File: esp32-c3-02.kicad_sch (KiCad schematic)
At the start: 30 parts, among them J3 GSD090012SEU, U3 ESP32-C3-WROOM-02-H4, U4 CP2102N-Axx-xQFN20, U5 USBLC6-2SC6, U6 W25Q32JVSSIQ

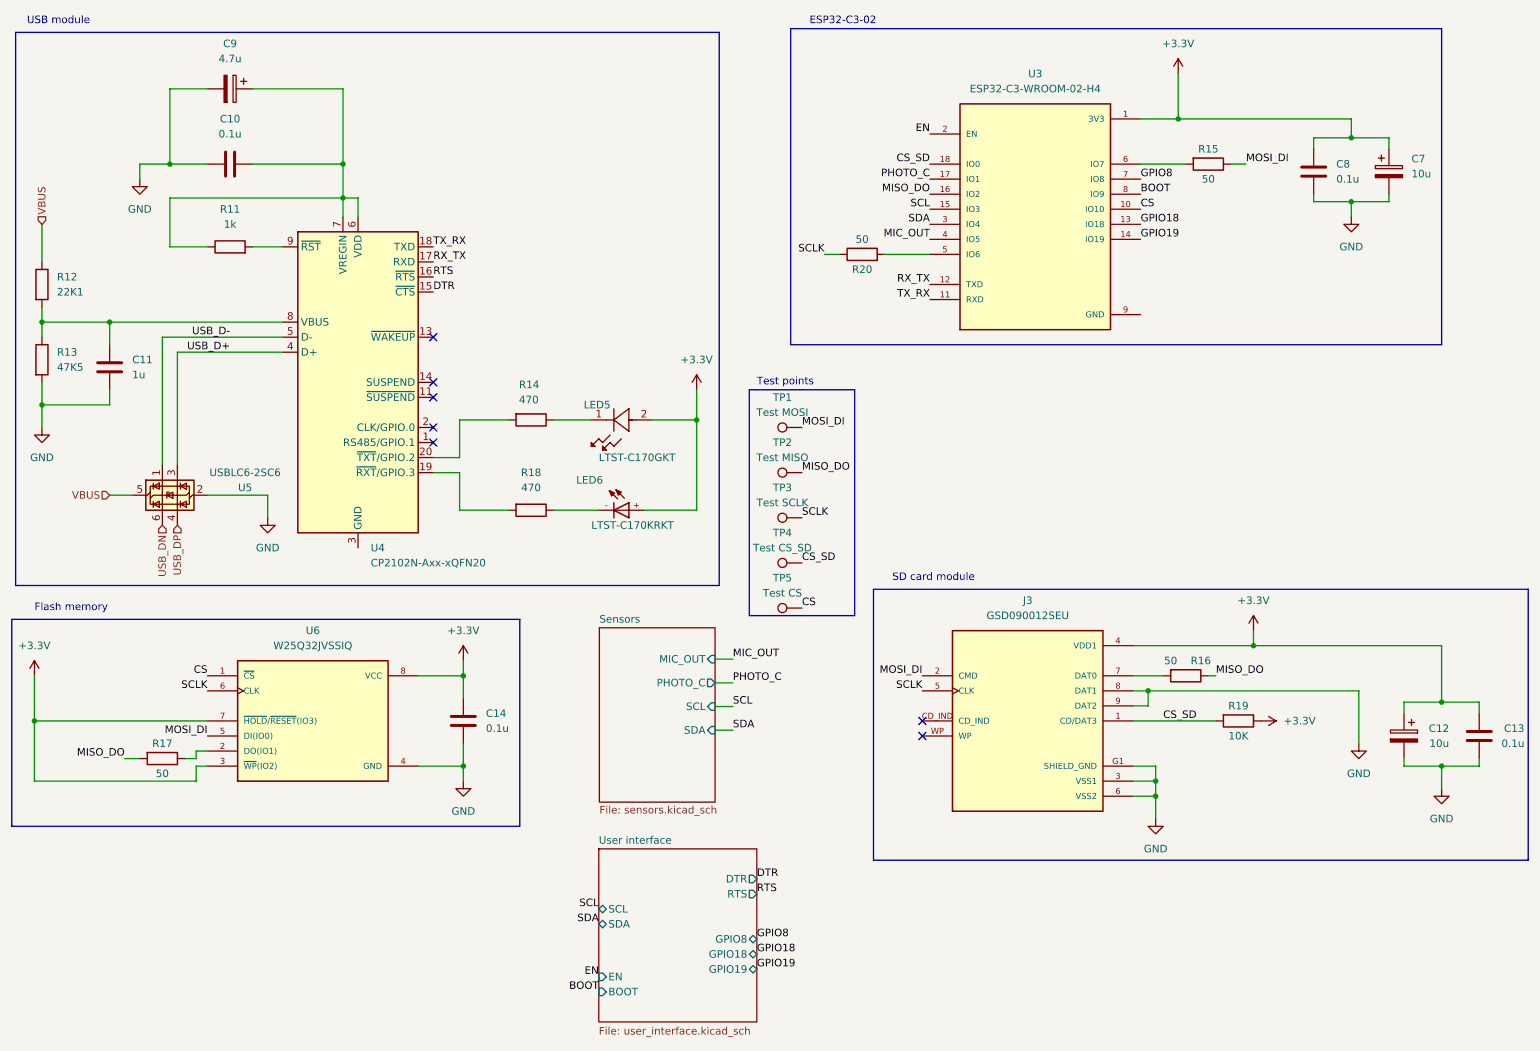
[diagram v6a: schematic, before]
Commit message: 1.3.4 Electrical Rules Check
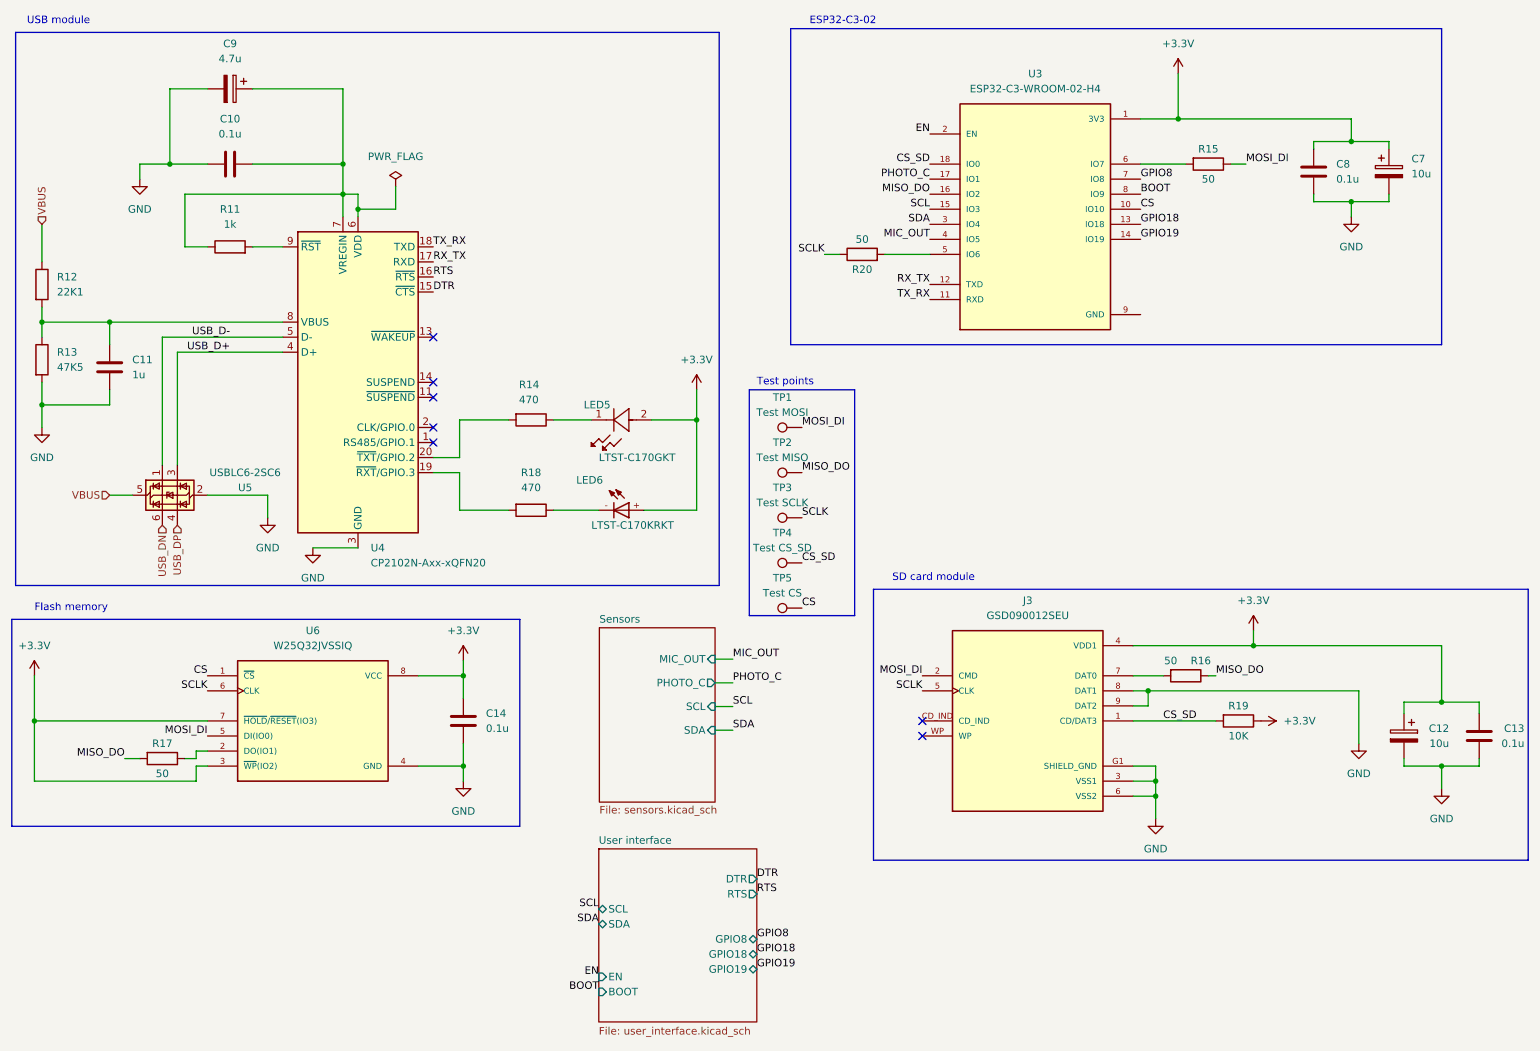
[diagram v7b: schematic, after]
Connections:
- net GND: now also U4.12 (GND), U4.21 (GND), U4.3 (GND)
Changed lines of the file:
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@@
 	)
 	(junction
-		(at 76.2 50.165)
-		(diameter 0)
-		(color 0 0 0 0)
-	)
-	(junction
 		(at 24.13 138.43)
 		(diameter 0)
@@
 	)
 	(junction
+		(at 78.74 52.07)
+		(diameter 0)
+		(color 0 0 0 0)
+	)
+	(junction
 		(at 213.36 148.59)
 		(diameter 0)
@@
 	)
 	(junction
-		(at 246.38 40.005)
+		(at 246.38 40.64)
 		(diameter 0)
 		(color 0 0 0 0)
@@
 	)
 	(junction
+		(at 76.2 49.53)
+		(diameter 0)
+		(color 0 0 0 0)
+	)
+	(junction
 		(at 135.89 87.63)
 		(diameter 0)
@@
 	(wire
 		(pts
+			(xy 76.2 49.53) (xy 76.2 53.34)
+		)
+		(stroke
+			(width 0)
+			(type default)
+		)
+	)
+	(wire
+		(pts
 			(xy 247.65 142.24) (xy 247.65 133.35)
 		)
@@
 	(wire
 		(pts
-			(xy 76.2 50.165) (xy 46.99 50.165)
+			(xy 76.2 49.53) (xy 49.53 49.53)
 		)
 		(stroke
@@
 	(wire
 		(pts
-			(xy 240.03 40.005) (xy 240.03 41.91)
+			(xy 240.03 40.64) (xy 240.03 41.91)
 		)
 		(stroke
@@
 	(wire
 		(pts
-			(xy 252.73 40.005) (xy 252.73 41.91)
+			(xy 252.73 40.64) (xy 252.73 41.91)
 		)
 		(stroke
@@
 	(wire
 		(pts
-			(xy 46.99 58.42) (xy 53.34 58.42)
+			(xy 49.53 58.42) (xy 53.34 58.42)
 		)
 		(stroke
@@
 	(wire
 		(pts
-			(xy 46.99 50.165) (xy 46.99 58.42)
+			(xy 49.53 49.53) (xy 49.53 58.42)
 		)
 		(stroke
@@
 	(wire
 		(pts
-			(xy 76.2 50.165) (xy 78.74 50.165)
+			(xy 76.2 49.53) (xy 78.74 49.53)
 		)
 		(stroke
@@
 	(wire
 		(pts
-			(xy 78.74 50.165) (xy 78.74 53.34)
+			(xy 78.74 52.07) (xy 78.74 53.34)
 		)
 		(stroke
@@
 	(wire
 		(pts
-			(xy 240.03 40.005) (xy 246.38 40.005)
+			(xy 240.03 40.64) (xy 246.38 40.64)
 		)
 		(stroke
@@
 	(wire
 		(pts
+			(xy 71.12 109.22) (xy 78.74 109.22)
+		)
+		(stroke
+			(width 0)
+			(type default)
+		)
+	)
+	(wire
+		(pts
 			(xy 25.4 81.28) (xy 25.4 85.09)
 		)
@@
 	(wire
 		(pts
-			(xy 246.38 40.005) (xy 252.73 40.005)
+			(xy 246.38 40.64) (xy 252.73 40.64)
+		)
+		(stroke
+			(width 0)
+			(type default)
+		)
+	)
+	(wire
+		(pts
+			(xy 85.09 48.26) (xy 85.09 52.07)
 		)
 		(stroke
@@
 	(wire
 		(pts
+			(xy 85.09 52.07) (xy 78.74 52.07)
+		)
+		(stroke
+			(width 0)
+			(type default)
+		)
+	)
+	(wire
+		(pts
 			(xy 91.44 93.98) (xy 95.885 93.98)
 		)
@@
 	(wire
 		(pts
-			(xy 246.38 36.83) (xy 246.38 40.005)
+			(xy 246.38 36.83) (xy 246.38 40.64)
 		)
 		(stroke
@@
 	(wire
 		(pts
-			(xy 76.2 53.34) (xy 76.2 50.165)
+			(xy 51.435 148.59) (xy 51.435 146.05)
 		)
 		(stroke
@@
 	(wire
 		(pts
-			(xy 51.435 148.59) (xy 51.435 146.05)
+			(xy 76.2 44.45) (xy 76.2 49.53)
 		)
 		(stroke
@@
 	(wire
 		(pts
-			(xy 76.2 44.45) (xy 76.2 50.165)
+			(xy 212.09 135.89) (xy 212.09 133.35)
 		)
 		(stroke
@@
 	(wire
 		(pts
-			(xy 212.09 135.89) (xy 212.09 133.35)
+			(xy 135.89 82.55) (xy 135.89 87.63)
 		)
 		(stroke
@@
 	(wire
 		(pts
-			(xy 135.89 82.55) (xy 135.89 87.63)
+			(xy 167.64 59.69) (xy 175.26 59.69)
 		)
 		(stroke
@@
 	(wire
 		(pts
-			(xy 167.64 59.69) (xy 175.26 59.69)
+			(xy 240.03 50.8) (xy 246.38 50.8)
 		)
 		(stroke
@@
 	(wire
 		(pts
-			(xy 240.03 50.8) (xy 246.38 50.8)
+			(xy 78.74 49.53) (xy 78.74 52.07)
 		)
 		(stroke
@@
 	)
 	(symbol
+		(lib_id "power:PWR_FLAG")
+		(at 85.09 48.26 0)
+		(unit 1)
+		(exclude_from_sim no)
+		(in_bom yes)
+		(on_board yes)
+		(dnp no)
+		(fields_autoplaced yes)
+		(property "Reference" "#FLG04"
+			(at 85.09 46.355 0)
+			(effects
+				(font
+					(size 1.27 1.27)
+				)
+				(hide yes)
+			)
+		)
+		(property "Value" "PWR_FLAG"
+			(at 85.09 43.18 0)
+			(effects
+				(font
+					(size 1.27 1.27)
+				)
+			)
+		)
+		(property "Footprint" ""
+			(at 85.09 48.26 0)
+			(effects
+				(font
+					(size 1.27 1.27)
+				)
+				(hide yes)
+			)
+		)
+		(property "Datasheet" "~"
+			(at 85.09 48.26 0)
+			(effects
+				(font
+					(size 1.27 1.27)
+				)
+				(hide yes)
+			)
+		)
+		(property "Description" "Special symbol for telling ERC where power comes from"
+			(at 85.09 48.26 0)
+			(effects
+				(font
+					(size 1.27 1.27)
+				)
+				(hide yes)
+			)
+		)
+		(pin "1"
+		)
+		(instances
+			(project ""
+				(path "/4f22731a-f223-4edc-b2be-2233ce3b179a/018e42ea-250a-4271-8f17-dfb169b11a85"
+					(reference "#FLG04")
+					(unit 1)
+				)
+			)
+		)
+	)
+	(symbol
 		(lib_id "GSD090012SEU:GSD090012SEU")
 		(at 191.77 138.43 0)
@@
 					(unit 1)
 				)
+			)
+		)
+	)
+	(symbol
+		(lib_id "power:GND")
+		(at 71.12 109.22 0)
+		(unit 1)
+		(exclude_from_sim no)
+		(in_bom yes)
+		(on_board yes)
+		(dnp no)
+		(fields_autoplaced yes)
+		(property "Reference" "#PWR055"
+			(at 71.12 115.57 0)
+			(effects
+				(font
+					(size 1.27 1.27)
+				)
+				(hide yes)
+			)
+		)
+		(property "Value" "GND"
+			(at 71.12 114.3 0)
+			(effects
+				(font
+					(size 1.27 1.27)
+				)
+			)
+		)
+		(property "Footprint" ""
+			(at 71.12 109.22 0)
+			(effects
+				(font
+					(size 1.27 1.27)
+				)
+				(hide yes)
+			)
+		)
+		(property "Datasheet" ""
+			(at 71.12 109.22 0)
+			(effects
+				(font
+					(size 1.27 1.27)
+				)
+				(hide yes)
+			)
+		)
+		(property "Description" "Power symbol creates a global label with name \"GND\" , ground"
+			(at 71.12 109.22 0)
+			(effects
+				(font
+					(size 1.27 1.27)
+				)
+				(hide yes)
+			)
+		)
+		(pin "1"
+		)
+		(instances
+			(project "project5_esp32_demo_project"
+				(path "/4f22731a-f223-4edc-b2be-2233ce3b179a/018e42ea-250a-4271-8f17-dfb169b11a85"
+					(reference "#PWR055")
+					(unit 1)
+				)

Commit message: 1.3.9 Bring remaining components to the layout editor
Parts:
- J3: footprint GSD090012SEU:AMPHENOL_GSD090012SEU -> ESP32_demo_project:GSD090012SEU
- LED5: footprint (none) -> ESP32_demo_project:LTST-C170GKT
- LED6: footprint LTST-C170KRKT:DIOC200X125X110 -> ESP32_demo_project:LTST-C170KRKT
- U3: footprint ESP32-C3-WROOM-02-H4:MODULE_ESP32-C3-WROOM-02-H4 -> ESP32_demo_project:ESP32-C3-WROOM-02-H4
- U4: footprint Package_DFN_QFN:SiliconLabs_QFN-20-1EP_3x3mm_P0.5mm -> ESP32_demo_project:QFN20_CP2102N_SIL
- U6: footprint W25Q32JVSSIQ:SOIC127P790X216-8N -> ESP32_demo_project:W25Q32JVSSIQ
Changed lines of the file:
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@@
 			)
 		)
-		(property "Footprint" "GSD090012SEU:AMPHENOL_GSD090012SEU"
+		(property "Footprint" "ESP32_demo_project:GSD090012SEU"
 			(at 191.77 138.43 0)
 			(effects
@@
 			)
 		)
-		(property "Footprint" "Package_DFN_QFN:SiliconLabs_QFN-20-1EP_3x3mm_P0.5mm"
+		(property "Footprint" "ESP32_demo_project:QFN20_CP2102N_SIL"
 			(at 110.49 107.95 0)
 			(effects
@@
 			)
 		)
-		(property "Footprint" "LTST-C170KRKT:DIOC200X125X110"
+		(property "Footprint" "ESP32_demo_project:LTST-C170KRKT"
 			(at 121.92 102.87 0)
 			(effects
@@
 			)
 		)
-		(property "Footprint" "W25Q32JVSSIQ:SOIC127P790X216-8N"
+		(property "Footprint" "ESP32_demo_project:W25Q32JVSSIQ"
 			(at 71.12 138.43 0)
 			(effects
@@
 			)
 		)
-		(property "Footprint" "ESP32-C3-WROOM-02-H4:MODULE_ESP32-C3-WROOM-02-H4"
+		(property "Footprint" "ESP32_demo_project:ESP32-C3-WROOM-02-H4"
 			(at 193.04 54.61 0)
 			(effects
@@
 			)
 		)
-		(property "Footprint" ""
+		(property "Footprint" "ESP32_demo_project:LTST-C170GKT"
 			(at 128.27 87.63 0)
 			(effects
